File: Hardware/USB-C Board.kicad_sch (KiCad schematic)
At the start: 45 parts, among them J1 USB_C_Receptacle_USB2.0, J2 Conn_01x04_Male, J3 Conn_01x02_Male, J4 Conn_01x02_Male, J5 Conn_01x02_Male, J9 Conn_01x04_MountingPin, Q1 DMP3013SFV, SW1 SW_Push, U1 AMS1117-3.3, U3 STUSB4500QTR

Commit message: footprint tweaks...
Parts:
- J2: footprint Connector_PinHeader_2.54mm:PinHeader_1x04_P2.54mm_Vertical -> Tinker:PinHeader_1x04_P2.54mm_Vertical
- J3, J4, J5: footprint Connector_PinHeader_2.54mm:PinHeader_1x02_P2.54mm_Vertical -> Tinker:PinHeader_1x02_P2.54mm_Vertical
- U1: footprint Package_TO_SOT_SMD:SOT-223-3_TabPin2 -> Tinker:SOT-223-3_TabPin2
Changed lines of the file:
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@@
     (property "Reference" "J3" (id 0) (at 80.645 111.76 0))
     (property "Value" "Conn_01x02_Male" (id 1) (at 80.645 114.3 0))
-    (property "Footprint" "Connector_PinHeader_2.54mm:PinHeader_1x02_P2.54mm_Vertical" (id 2) (at 81.28 116.84 0)
+    (property "Footprint" "Tinker:PinHeader_1x02_P2.54mm_Vertical" (id 2) (at 81.28 116.84 0)
       (effects (font (size 1.27 1.27)) hide)
     )
@@
     (property "Reference" "U1" (id 0) (at 36.83 166.5732 0))
     (property "Value" "AMS1117-3.3" (id 1) (at 36.83 168.8846 0))
-    (property "Footprint" "Package_TO_SOT_SMD:SOT-223-3_TabPin2" (id 2) (at 36.83 167.64 0)
+    (property "Footprint" "Tinker:SOT-223-3_TabPin2" (id 2) (at 36.83 167.64 0)
       (effects (font (size 1.27 1.27)) hide)
     )
@@
     (property "Reference" "J4" (id 0) (at 80.645 127 0))
     (property "Value" "Conn_01x02_Male" (id 1) (at 80.645 129.54 0))
-    (property "Footprint" "Connector_PinHeader_2.54mm:PinHeader_1x02_P2.54mm_Vertical" (id 2) (at 81.28 132.08 0)
+    (property "Footprint" "Tinker:PinHeader_1x02_P2.54mm_Vertical" (id 2) (at 81.28 132.08 0)
       (effects (font (size 1.27 1.27)) hide)
     )
@@
       (effects (font (size 1.27 1.27)) (justify right))
     )
-    (property "Footprint" "Connector_PinHeader_2.54mm:PinHeader_1x04_P2.54mm_Vertical" (id 2) (at 53.34 78.74 0)
+    (property "Footprint" "Tinker:PinHeader_1x04_P2.54mm_Vertical" (id 2) (at 53.34 78.74 0)
       (effects (font (size 1.27 1.27)) hide)
     )
@@
     (property "Reference" "J5" (id 0) (at 84.455 166.37 0))
     (property "Value" "Conn_01x02_Male" (id 1) (at 84.455 168.91 0))
-    (property "Footprint" "Connector_PinHeader_2.54mm:PinHeader_1x02_P2.54mm_Vertical" (id 2) (at 85.09 171.45 0)
+    (property "Footprint" "Tinker:PinHeader_1x02_P2.54mm_Vertical" (id 2) (at 85.09 171.45 0)
       (effects (font (size 1.27 1.27)) hide)
     )
@@
     )
     (path "/ce562b82-4d15-4512-9ef8-80a89b06889d"
-      (reference "J2") (unit 1) (value "Conn_01x04_Male") (footprint "Connector_PinHeader_2.54mm:PinHeader_1x04_P2.54mm_Vertical")
+      (reference "J2") (unit 1) (value "Conn_01x04_Male") (footprint "Tinker:PinHeader_1x04_P2.54mm_Vertical")
     )
     (path "/31399746-8e56-4d74-b787-07c634e0c687"
-      (reference "J3") (unit 1) (value "Conn_01x02_Male") (footprint "Connector_PinHeader_2.54mm:PinHeader_1x02_P2.54mm_Vertical")
+      (reference "J3") (unit 1) (value "Conn_01x02_Male") (footprint "Tinker:PinHeader_1x02_P2.54mm_Vertical")
     )
     (path "/866e0145-9665-41b4-abc2-4ab89f1e24e6"
-      (reference "J4") (unit 1) (value "Conn_01x02_Male") (footprint "Connector_PinHeader_2.54mm:PinHeader_1x02_P2.54mm_Vertical")
+      (reference "J4") (unit 1) (value "Conn_01x02_Male") (footprint "Tinker:PinHeader_1x02_P2.54mm_Vertical")
     )
     (path "/fb3406f1-7439-4c3c-b07d-423418b2c3c6"
-      (reference "J5") (unit 1) (value "Conn_01x02_Male") (footprint "Connector_PinHeader_2.54mm:PinHeader_1x02_P2.54mm_Vertical")
+      (reference "J5") (unit 1) (value "Conn_01x02_Male") (footprint "Tinker:PinHeader_1x02_P2.54mm_Vertical")
     )
     (path "/ae69f442-7b32-4ab2-972d-28d283e0750f"
@@
     )
     (path "/7666fe9f-4f0d-42ff-bbc9-1c1e12969d3f"
-      (reference "U1") (unit 1) (value "AMS1117-3.3") (footprint "Package_TO_SOT_SMD:SOT-223-3_TabPin2")
+      (reference "U1") (unit 1) (value "AMS1117-3.3") (footprint "Tinker:SOT-223-3_TabPin2")
     )
     (path "/d2d1f0f1-2045-47df-a1ba-ea7035f406a6"

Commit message: s'more tweakin'
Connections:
- net 3v3 renamed Vsec
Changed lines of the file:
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@@
     )
   )
-  (global_label "3v3" (shape input) (at 48.26 167.64 0) (fields_autoplaced)
+  (global_label "Vsec" (shape input) (at 48.26 167.64 0) (fields_autoplaced)
     (effects (font (size 1.27 1.27)) (justify left))
-    (property "Intersheet References" "${INTERSHEET_REFS}" (id 0) (at 54.0598 167.5606 0)
+    (property "Intersheet References" "${INTERSHEET_REFS}" (id 0) (at 54.9669 167.5606 0)
       (effects (font (size 1.27 1.27)) (justify left) hide)
     )
@@
     )
   )
-  (global_label "3v3" (shape input) (at 80.01 171.45 180) (fields_autoplaced)
+  (global_label "Vsec" (shape input) (at 80.01 171.45 180) (fields_autoplaced)
     (effects (font (size 1.27 1.27)) (justify right))
-    (property "Intersheet References" "${INTERSHEET_REFS}" (id 0) (at 74.2102 171.5294 0)
+    (property "Intersheet References" "${INTERSHEET_REFS}" (id 0) (at 73.3031 171.3706 0)
       (effects (font (size 1.27 1.27)) (justify right) hide)
     )

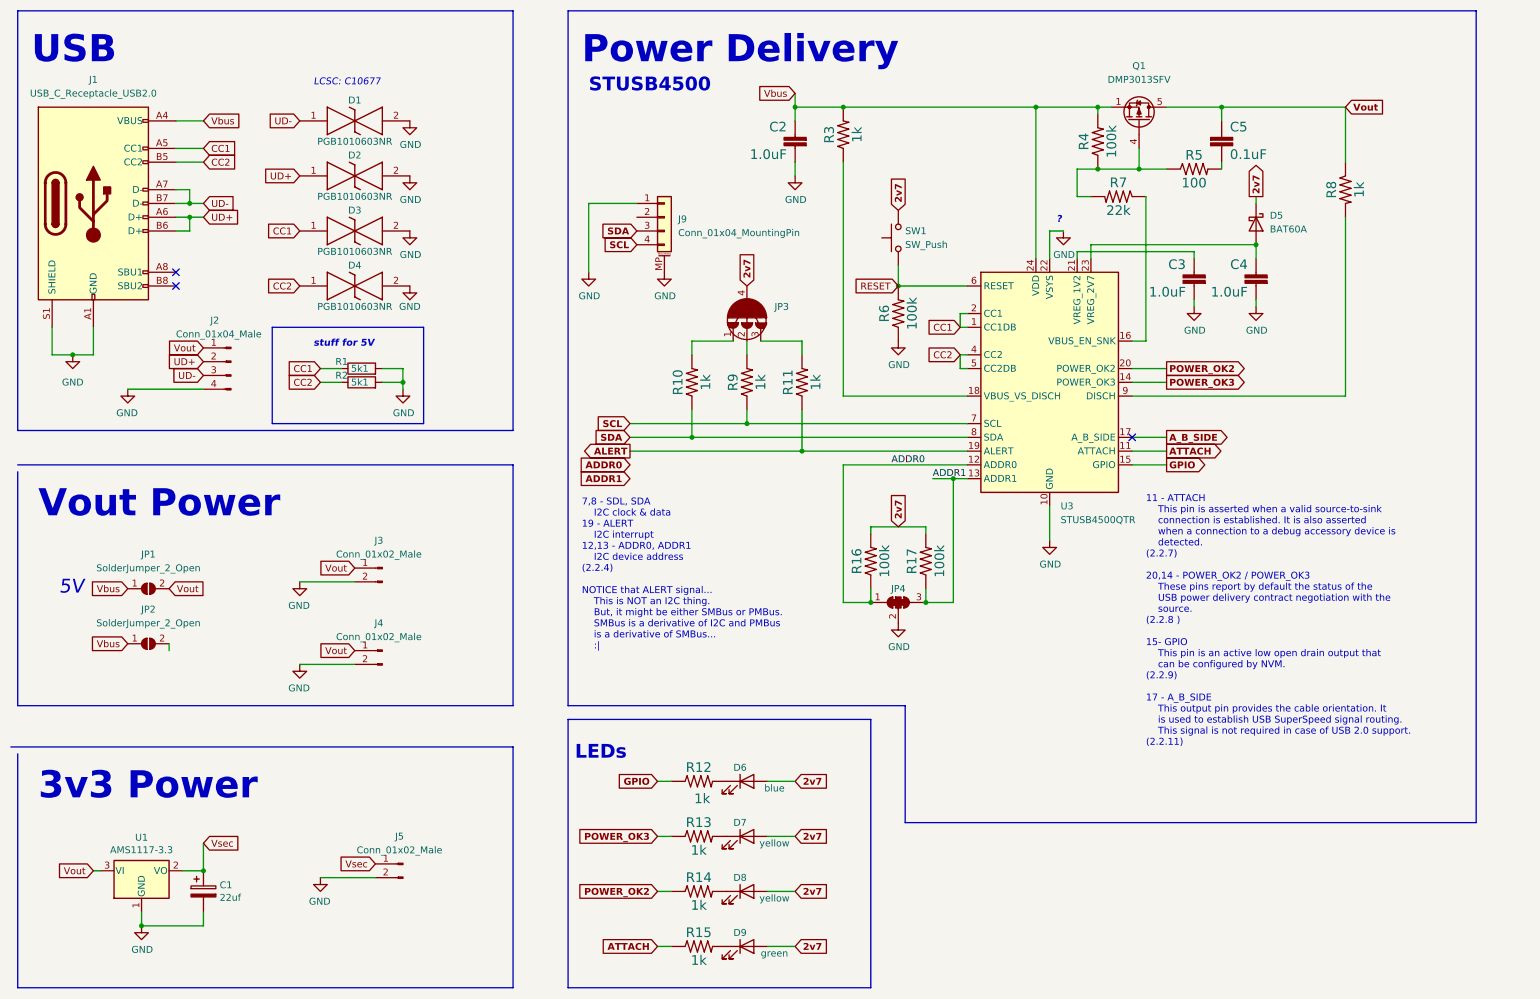
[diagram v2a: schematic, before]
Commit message: Added empty controller board
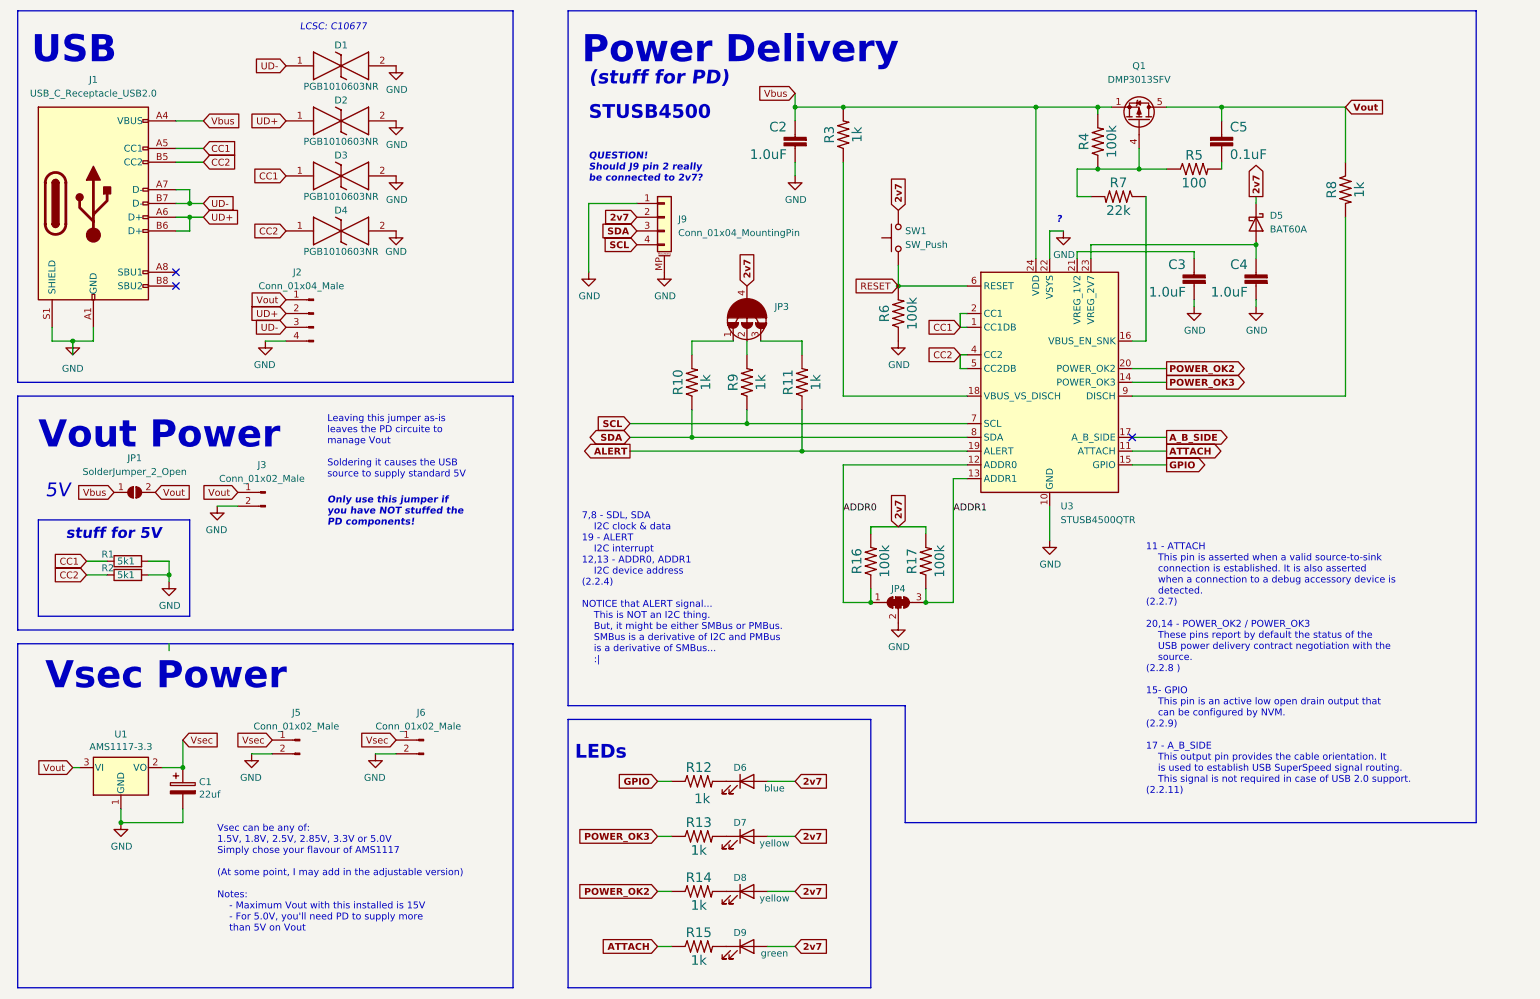
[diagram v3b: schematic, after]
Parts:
- removed J4: Conn_01x02_Male, Tinker:PinHeader_1x02_P2.54mm_Vertical, symbol Connector:Conn_01x02_Male
- removed JP2: SolderJumper_2_Open, Tinker:SolderJumper-2_P1.3mm_Open_RoundedPad1.0x1.5mm, symbol Jumper:SolderJumper_2_Open
- added J6: Conn_01x02_Male, Tinker:PinHeader_1x02_P2.54mm_Vertical, symbol Connector:Conn_01x02_Male
- J9: footprint Connector_JST:JST_SH_BM04B-SRSS-TB_1x04-1MP_P1.00mm_Vertical -> Tinker:JST_SH_SM04B-SRSS-TB_1x04-1MP_P1.00mm_Horizontal
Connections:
- net 2v7: now also J9.2 (Pin_2)
- net GND: now also J6.2 (Pin_2)
- net Vsec: now also J6.1 (Pin_1)
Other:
- note added: "(stuff for PD)"
- note added: "Leaving this jumper as-is leaves the PD circuite to manage Vout Soldering it causes the USB source to supply standard 5V"
- note added: "Only use this jumper if you have NOT stuffed the PD components!"
- note added: "QUESTION! Should J9 pin 2 really be connected to 2v7?"
- note added: "Vsec Power"
- note added: "Vsec can be any of: 1.5V, 1.8V, 2.5V, 2.85V, 3.3V or 5.0V Simply chose your flavour of AMS1117 (At some point, I may add in the adjustable version) Notes: - Maximum Vout with this installed is 15V - For 5.0V, you'll need PD to supply more than 5V on Vout"
- note removed: "3v3 Power"
- moved on the sheet: C1, D1, D2, D3, D4, J2, J3, J5, JP1, R1, R2, U1

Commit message: ...
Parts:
- added J4: Conn_01x02_Male, Tinker:PinHeader_1x02_P2.54mm_Vertical, symbol Connector:Conn_01x02_Male
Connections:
- net GND: now also J4.2 (Pin_2)
- net Vout: now also J4.1 (Pin_1)
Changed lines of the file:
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@@
+    (stroke (width 0) (type default) (color 0 0 0 0))
+  )
+  (wire (pts (xy 54.61 119.38) (xy 50.8 119.38))
     (stroke (width 0) (type default) (color 0 0 0 0))
   )
@@
     (effects (font (size 1.27 1.27)) (justify right))
     (property "Intersheet References" "${INTERSHEET_REFS}" (id 0) (at 56.914 72.4694 0)
+      (effects (font (size 1.27 1.27)) (justify right) hide)
+    )
+  )
+  (global_label "Vout" (shape input) (at 54.61 116.84 180) (fields_autoplaced)
+    (effects (font (size 1.27 1.27)) (justify right))
+    (property "Intersheet References" "${INTERSHEET_REFS}" (id 0) (at 48.0845 116.7606 0)
       (effects (font (size 1.27 1.27)) (justify right) hide)
     )
@@
     (pin "2")
   )
+  (symbol (lib_id "Connector:Conn_01x02_Male") (at 59.69 116.84 0) (mirror y) (unit 1)
+    (in_bom yes) (on_board yes)
+    (property "Reference" "J4" (id 0) (at 59.055 111.76 0))
+    (property "Value" "Conn_01x02_Male" (id 1) (at 59.055 114.3 0))
+    (property "Footprint" "Tinker:PinHeader_1x02_P2.54mm_Vertical" (id 2) (at 59.69 116.84 0)
+      (effects (font (size 1.27 1.27)) hide)
+    )
+    (property "Datasheet" "~" (id 3) (at 59.69 116.84 0)
+      (effects (font (size 1.27 1.27)) hide)
+    )
+    (pin "1")
+    (pin "2")
+  )
   (symbol (lib_id "power:GND") (at 83.82 44.45 0) (unit 1)
     (in_bom yes) (on_board yes)
@@
     (pin "1")
     (pin "2")
+  )
+  (symbol (lib_id "power:GND") (at 50.8 119.38 0) (mirror y) (unit 1)
+    (in_bom yes) (on_board yes)
+    (property "Reference" "#PWR0110" (id 0) (at 50.8 125.73 0)
+      (effects (font (size 1.27 1.27)) hide)
+    )
+    (property "Value" "GND" (id 1) (at 50.673 123.7742 0))
+    (property "Footprint" "" (id 2) (at 50.8 119.38 0)
+      (effects (font (size 1.27 1.27)) hide)
+    )
+    (property "Datasheet" "" (id 3) (at 50.8 119.38 0)
+      (effects (font (size 1.27 1.27)) hide)
+    )
+    (pin "1")
   )
   (symbol (lib_id "SparkFun_STUSB4500_USB-PD-eagle-import:0.1UF-0603-100V-10%") (at 236.22 39.37 0) (unit 1)
@@
       (reference "#PWR0109") (unit 1) (value "GND") (footprint "")
     )
+    (path "/8c4e211c-0dcb-4cc8-90e4-1b0e164dea0d"
+      (reference "#PWR0110") (unit 1) (value "GND") (footprint "")
+    )
     (path "/7a61b459-0a7f-4216-98ba-dce359d99263"
       (reference "#PWR0112") (unit 1) (value "GND") (footprint "")
@@
       (reference "J3") (unit 1) (value "Conn_01x02_Male") (footprint "Tinker:PinHeader_1x02_P2.54mm_Vertical")
     )
+    (path "/4b9f3ca1-fb99-4af6-a9fd-ecb98c706083"
+      (reference "J4") (unit 1) (value "Conn_01x02_Male") (footprint "Tinker:PinHeader_1x02_P2.54mm_Vertical")
+    )
     (path "/fb3406f1-7439-4c3c-b07d-423418b2c3c6"

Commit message: .........
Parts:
- removed J9: Conn_01x04_MountingPin, Tinker:JST_SH_SM04B-SRSS-TB_1x04-1MP_P1.00mm_Horizontal, symbol Connector_Generic_MountingPin:Conn_01x04_MountingPin
- added J9: QWIIC_Stackable, Tinker:QWIIC_Stackable, symbol Connector_QWIIC_Stackable:QWIIC_Stackable
- C1: footprint Capacitor_Tantalum_SMD:CP_EIA-6032-28_Kemet-C_Pad2.25x2.35mm_HandSolder -> Tinker:CP_EIA-6032-28-Tantalumm_HandSolder
- JP1, JP3, JP4: now left out of the parts list
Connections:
- net 2v7: now also J9.2 (Pin_2)
- net GND: now also J9.1 (Pin_1), J9.MP (MountPin)
- net SCL: now also J9.4 (Pin_4)
- net SDA: now also J9.3 (Pin_3)
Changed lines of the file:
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@@
   )
   (symbol (lib_id "Jumper:SolderJumper_3_Bridged123") (at 176.53 123.19 0) (unit 1)
-    (in_bom yes) (on_board yes)
+    (in_bom no) (on_board yes)
     (property "Reference" "JP4" (id 0) (at 176.53 120.65 0))
     (property "Value" "SolderJumper_3_Bridged123" (id 1) (at 176.53 119.38 0)
@@
     (pin "2")
     (pin "3")
+  )
+  (symbol (lib_id "Connector_QWIIC_Stackable:QWIIC_Stackable") (at 133.35 52.07 0) (unit 1)
+    (in_bom yes) (on_board yes) (fields_autoplaced)
+    (property "Reference" "J9" (id 0) (at 135.89 52.4255 0)
+      (effects (font (size 1.27 1.27)) (justify left))
+    )
+    (property "Value" "QWIIC_Stackable" (id 1) (at 135.89 54.9655 0)
+      (effects (font (size 1.27 1.27)) (justify left))
+    )
+    (property "Footprint" "Tinker:QWIIC_Stackable" (id 2) (at 134.62 62.23 0)
+      (effects (font (size 1.27 1.27)) (justify left) hide)
+    )
+    (property "Datasheet" "~" (id 3) (at 133.35 52.07 0)
+      (effects (font (size 1.27 1.27)) hide)
+    )
+    (pin "1")
+    (pin "2")
+    (pin "3")
+    (pin "4")
+    (pin "MP")
   )
   (symbol (lib_id "Device:LED") (at 148.59 186.69 0) (unit 1)
@@
       (effects (font (size 1.27 1.27)) (justify left))
     )
-    (property "Footprint" "Capacitor_Tantalum_SMD:CP_EIA-6032-28_Kemet-C_Pad2.25x2.35mm_HandSolder" (id 2) (at 45.4152 161.29 0)
+    (property "Footprint" "Tinker:CP_EIA-6032-28-Tantalumm_HandSolder" (id 2) (at 45.4152 161.29 0)
       (effects (font (size 1.27 1.27)) hide)
     )
@@
   )
   (symbol (lib_id "Jumper:SolderJumper_2_Open") (at 35.56 102.87 0) (unit 1)
-    (in_bom yes) (on_board yes) (fields_autoplaced)
+    (in_bom no) (on_board yes) (fields_autoplaced)
     (property "Reference" "JP1" (id 0) (at 35.56 96.52 0))
     (property "Value" "SolderJumper_2_Open" (id 1) (at 35.56 99.06 0))
@@
     (pin "2")
   )
-  (symbol (lib_id "Connector_Generic_MountingPin:Conn_01x04_MountingPin") (at 133.35 52.07 0) (unit 1)
-    (in_bom yes) (on_board yes) (fields_autoplaced)
-    (property "Reference" "J9" (id 0) (at 135.89 52.4255 0)
-      (effects (font (size 1.27 1.27)) (justify left))
-    )
-    (property "Value" "Conn_01x04_MountingPin" (id 1) (at 135.89 54.9655 0)
-      (effects (font (size 1.27 1.27)) (justify left))
-    )
-    (property "Footprint" "Tinker:JST_SH_SM04B-SRSS-TB_1x04-1MP_P1.00mm_Horizontal" (id 2) (at 133.35 52.07 0)
-      (effects (font (size 1.27 1.27)) hide)
-    )
-    (property "Datasheet" "~" (id 3) (at 133.35 52.07 0)
-      (effects (font (size 1.27 1.27)) hide)
-    )
-    (pin "1")
-    (pin "2")
-    (pin "3")
-    (pin "4")
-    (pin "MP")
-  )
   (symbol (lib_id "Device:R") (at 34.29 115.57 90) (unit 1)
     (in_bom yes) (on_board yes)
@@
   )
   (symbol (lib_id "solderjumper_4_bridged_all:SolderJumper_4_Bridged") (at 148.59 71.12 0) (unit 1)
-    (in_bom yes) (on_board yes) (fields_autoplaced)
+    (in_bom no) (on_board yes) (fields_autoplaced)
     (property "Reference" "JP3" (id 0) (at 153.67 68.5934 0)
       (effects (font (size 1.27 1.27)) (justify left))
@@
     )
     (path "/3bace4ce-a868-4f09-9170-957904ae6c48"
-      (reference "C1") (unit 1) (value "22uf") (footprint "Capacitor_Tantalum_SMD:CP_EIA-6032-28_Kemet-C_Pad2.25x2.35mm_HandSolder")
+      (reference "C1") (unit 1) (value "22uf") (footprint "Tinker:CP_EIA-6032-28-Tantalumm_HandSolder")
     )
     (path "/1982ea30-43ab-48d7-b8a2-e0183faeedd2"
@@
       (reference "J6") (unit 1) (value "Conn_01x02_Male") (footprint "Tinker:PinHeader_1x02_P2.54mm_Vertical")
     )
-    (path "/ae69f442-7b32-4ab2-972d-28d283e0750f"
-      (reference "J9") (unit 1) (value "Conn_01x04_MountingPin") (footprint "Tinker:JST_SH_SM04B-SRSS-TB_1x04-1MP_P1.00mm_Horizontal")
+    (path "/06d274f4-343d-4463-9b40-01495b041e52"
+      (reference "J9") (unit 1) (value "QWIIC_Stackable") (footprint "Tinker:QWIIC_Stackable")
     )
     (path "/57968461-460a-478c-9a11-3b2cfae03e90"

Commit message: fiddlin' with stuff...
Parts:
- C2, C3, C4: symbol SparkFun_STUSB4500_USB-PD-eagle-import:1.0UF-0603-16V-10% -> Device:C
- C5: symbol SparkFun_STUSB4500_USB-PD-eagle-import:0.1UF-0603-100V-10% -> Device:C
- J1: Vendor (none) -> LCSC
- R10, R11, R12, R13, R14, R15, R3, R8, R9: symbol SparkFun_STUSB4500_USB-PD-eagle-import:1KOHM-0603-1/10W-1% -> Device:R_US
- R16, R17, R4, R6: symbol SparkFun_STUSB4500_USB-PD-eagle-import:100KOHM-0603-1/10W-1% -> Device:R_US
- R5: symbol SparkFun_STUSB4500_USB-PD-eagle-import:100OHM-0603-1/10W-1% -> Device:R_US
- R7: symbol SparkFun_STUSB4500_USB-PD-eagle-import:22KOHM-0603-1/10W-1% -> Device:R_US
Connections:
- net at Q1.4 (G), R4.1, R5.1: now also R7.1; no longer R7.2
- net at U3.16 (VBUS_EN_SNK): now also R7.2; no longer R7.1
